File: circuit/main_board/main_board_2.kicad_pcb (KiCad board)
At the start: 2 copper layers, 38 parts, among them J1 RJ45, J2 RJ45, J3 RJ45, J4 RJ45, J5 RJ45, J6 RJ45, J7 Screw_Terminal_01x02

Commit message: Finnished a complete first revision of the circuits
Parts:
- moved A4 23.9 mm to (125.8, 95.7)
- moved A5 23.9 mm to (125.8, 119.8)
- moved A6 23.9 mm to (125.8, 143.9)
- moved A1 23.9 mm to (81.3, 125.7)
- moved JO2_1 23.9 mm to (99.1, 128.3)
- moved JO2_3 23.9 mm to (99.1, 80.0)
- moved A2 23.9 mm to (81.3, 101.6)
- moved A3 23.9 mm to (81.3, 77.5)
- moved A7 23.9 mm to (93.3, 67.4)
- moved J7 23.9 mm to (70.0, 149.6)
- moved JI4 23.9 mm to (113.0, 44.5)
- moved JI6 23.9 mm to (123.2, 44.5)
- moved JO2_2 23.9 mm to (99.1, 104.1)
- moved JO4_1 23.9 mm to (99.1, 143.5)
- moved JO4_2 23.9 mm to (99.1, 119.4)
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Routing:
- net /LIM6: track 13.5 -> 223.7 mm
- net /LIM5: track 13.0 -> 195.1 mm
- net /LIM4: track 12.5 -> 156.4 mm
- net /LIM1: track 12.0 -> 117.2 mm
- net +5V: track 384.8 -> 467.3 mm
- net /LIM2: track 11.4 -> 85.1 mm
- net GND: track 269.8 -> 336.1 mm
- net Net-(A1-Pad6): track 34.5 -> 36.5 mm
- net Net-(A3-Pad6): track 34.5 -> 36.5 mm
- net Net-(A2-Pad6): track 34.5 -> 36.5 mm
- net Net-(A6-Pad6): track 34.5 -> 36.3 mm
- net Net-(A5-Pad6): track 34.5 -> 36.2 mm
- net /MS2: track 31.0 -> 29.9 mm

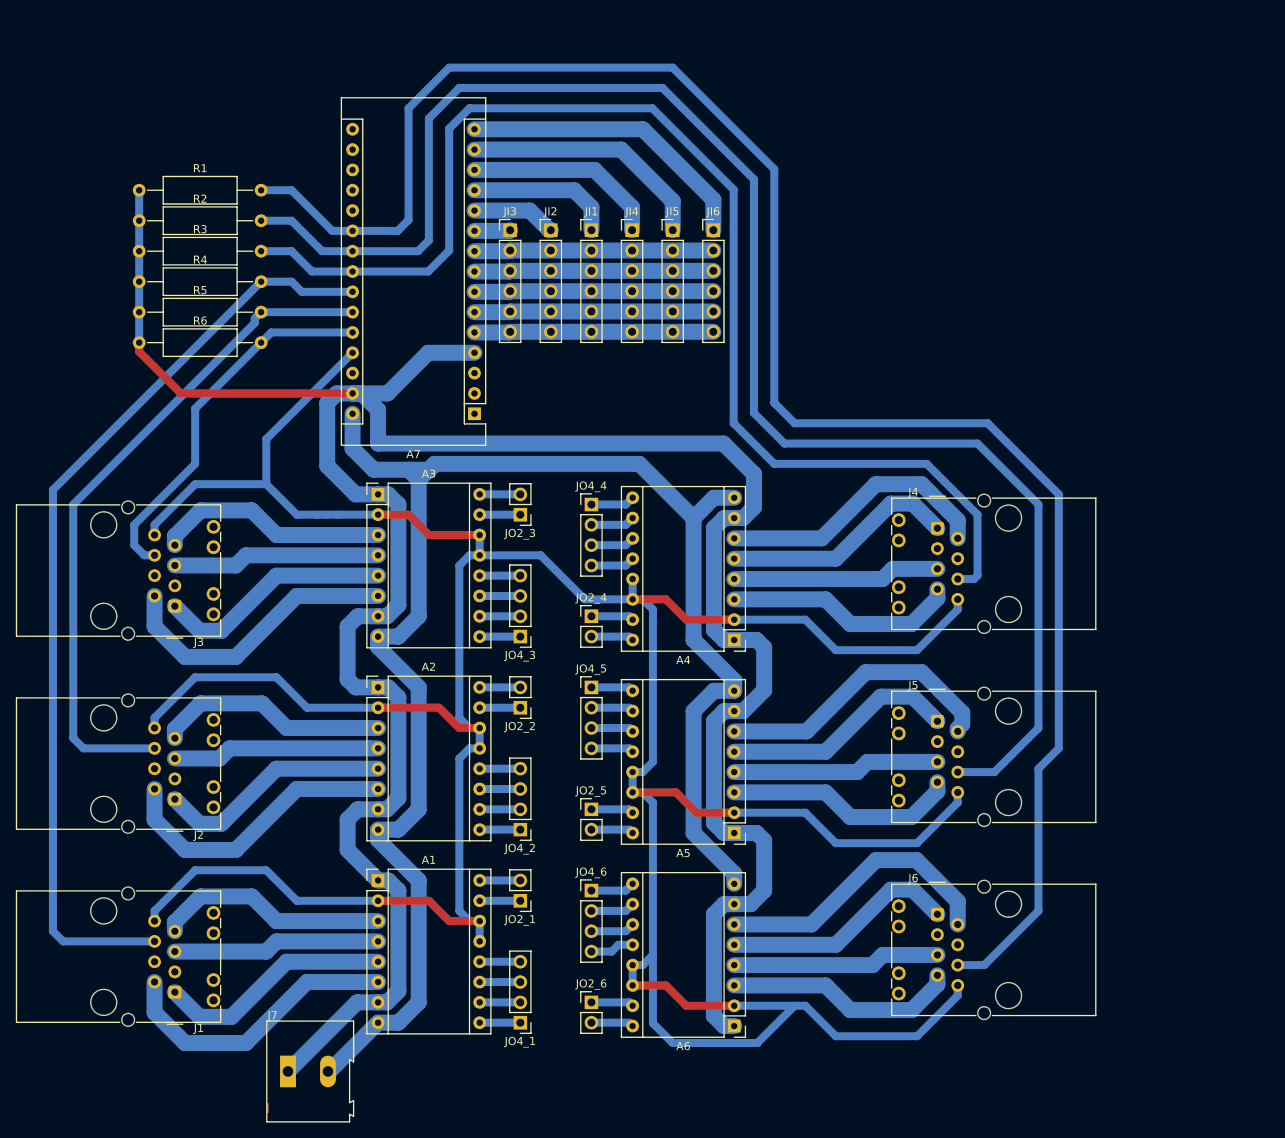
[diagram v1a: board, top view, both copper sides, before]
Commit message: Adjusted lane size
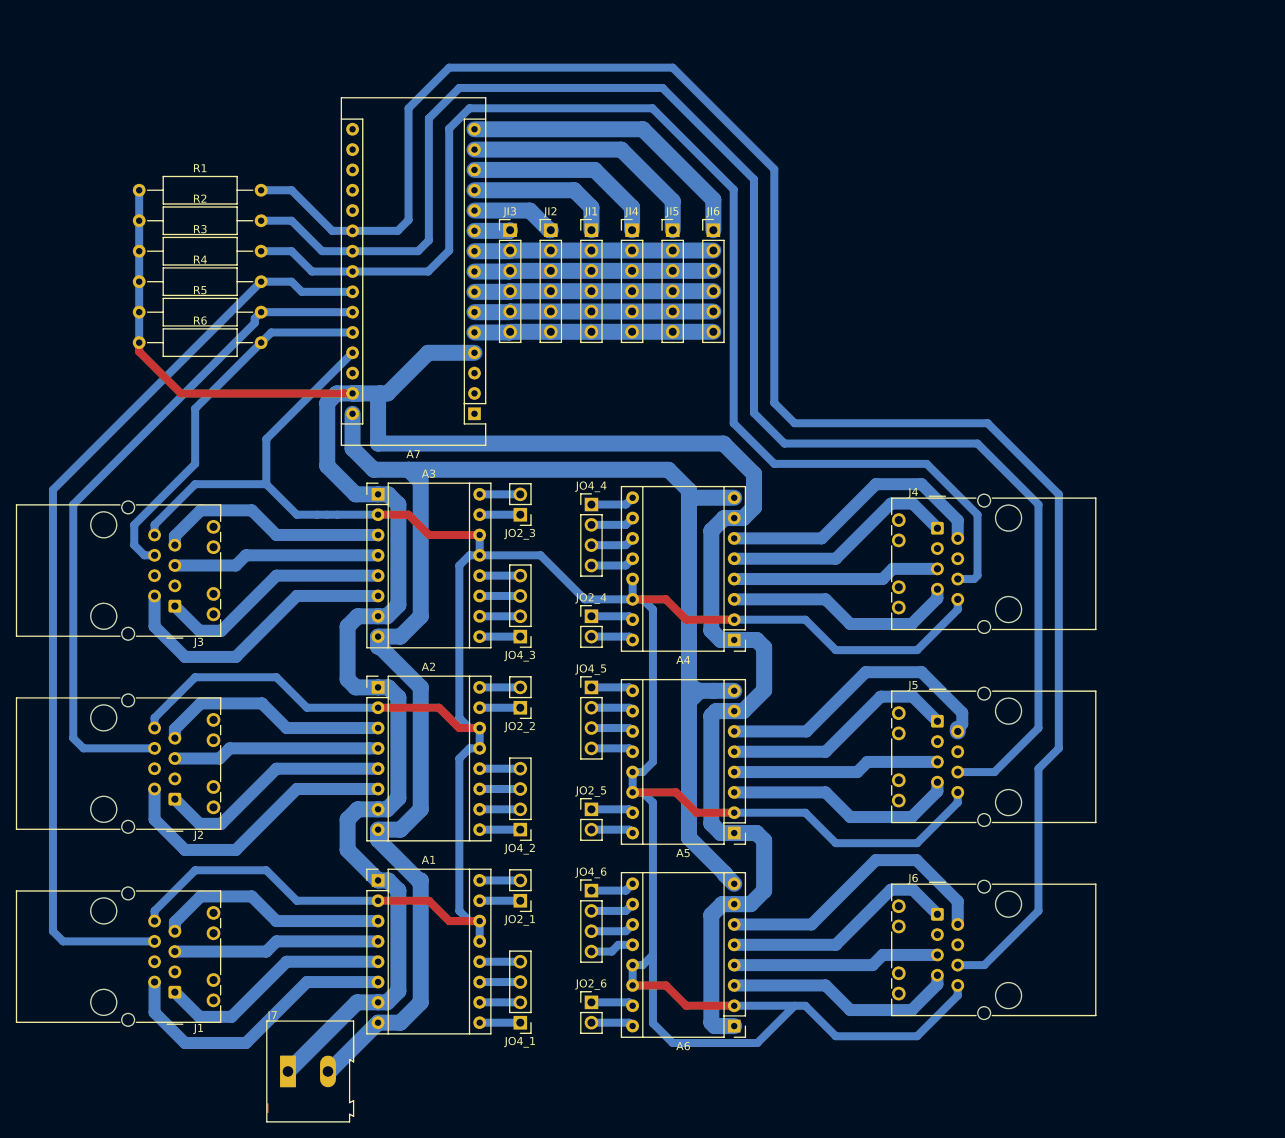
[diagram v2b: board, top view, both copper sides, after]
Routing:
- net GND: track 336.1 -> 338.1 mm
- net VCC: track 207.1 -> 208.6 mm

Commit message: Removed connection from sleep and reset to 5v
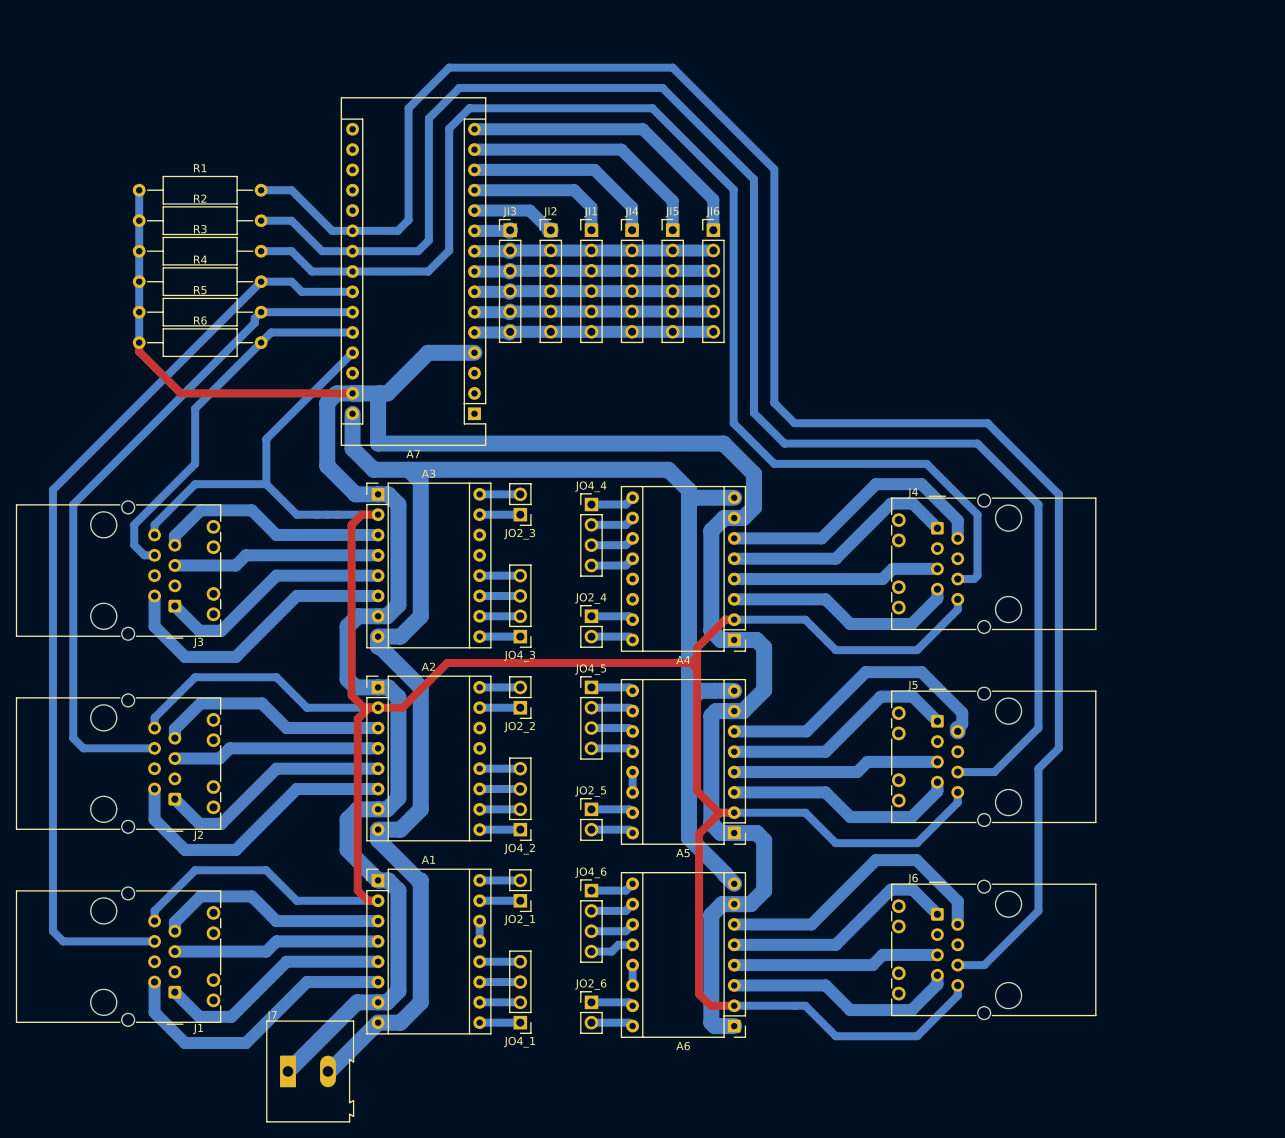
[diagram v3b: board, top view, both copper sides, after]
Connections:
- A1 pad 13: +5V -> Net-(A1-Pad13)
- A1 pad 14: +5V -> Net-(A1-Pad13)
- A2 pad 13: +5V -> Net-(A2-Pad13)
- A2 pad 14: +5V -> Net-(A2-Pad13)
- A3 pad 13: +5V -> Net-(A3-Pad13)
- A3 pad 14: +5V -> Net-(A3-Pad13)
- A4 pad 13: +5V -> Net-(A4-Pad13)
- A4 pad 14: +5V -> Net-(A4-Pad13)
- A5 pad 13: +5V -> Net-(A5-Pad13)
- A5 pad 14: +5V -> Net-(A5-Pad13)
- A6 pad 13: +5V -> Net-(A6-Pad13)
- A6 pad 14: +5V -> Net-(A6-Pad13)
- A7 pad 1: Net-(A7-Pad1) -> (no net)
- A7 pad 16: Net-(A7-Pad16) -> (no net)
- A7 pad 17: +3V3 -> (no net)
- A7 pad 18: Net-(A7-Pad18) -> (no net)
- A7 pad 19: Net-(A7-Pad19) -> (no net)
- A7 pad 2: Net-(A7-Pad2) -> (no net)
- A7 pad 20: Net-(A7-Pad20) -> (no net)
- A7 pad 28: Net-(A7-Pad28) -> (no net)
- A7 pad 3: Net-(A7-Pad3) -> (no net)
- J1 pad 3: Net-(J1-Pad3) -> (no net)
- J1 pad 4: Net-(J1-Pad4) -> (no net)
- J2 pad 3: Net-(J2-Pad3) -> (no net)
- J2 pad 4: Net-(J2-Pad4) -> (no net)
- J3 pad 3: Net-(J3-Pad3) -> (no net)
- J3 pad 4: Net-(J3-Pad4) -> (no net)
- J4 pad 3: Net-(J4-Pad3) -> (no net)
- J4 pad 4: Net-(J4-Pad4) -> (no net)
- J5 pad 3: Net-(J5-Pad3) -> (no net)
- J5 pad 4: Net-(J5-Pad4) -> (no net)
- J6 pad 3: Net-(J6-Pad3) -> (no net)
- J6 pad 4: Net-(J6-Pad4) -> (no net)
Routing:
- net +5V: track 467.3 -> 377.8 mm
- net Net-(A5-Pad13): track 0.00 -> 2.54 mm
- net Net-(A6-Pad13): track 0.00 -> 2.54 mm
- net Net-(A1-Pad13): track 0.00 -> 2.54 mm
- net GND: track 338.1 -> 337.1 mm
